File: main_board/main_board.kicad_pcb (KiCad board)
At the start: 2 copper layers, 116.1 x 100.1 mm, 52 parts, among them J1 USB3_A, J11 USB_C_Receptacle_USB2.0, J22 690-019-298-412, J3 Bus_M.2_Socket_M, SW1 Right angle Tact button, U1 AP3441SHE-7B, U12 RT9742SNGV, U2 ASEK-32.768KHZ-L-R-T, U5 74LVC1G07SE-7, U6 AP22653W6

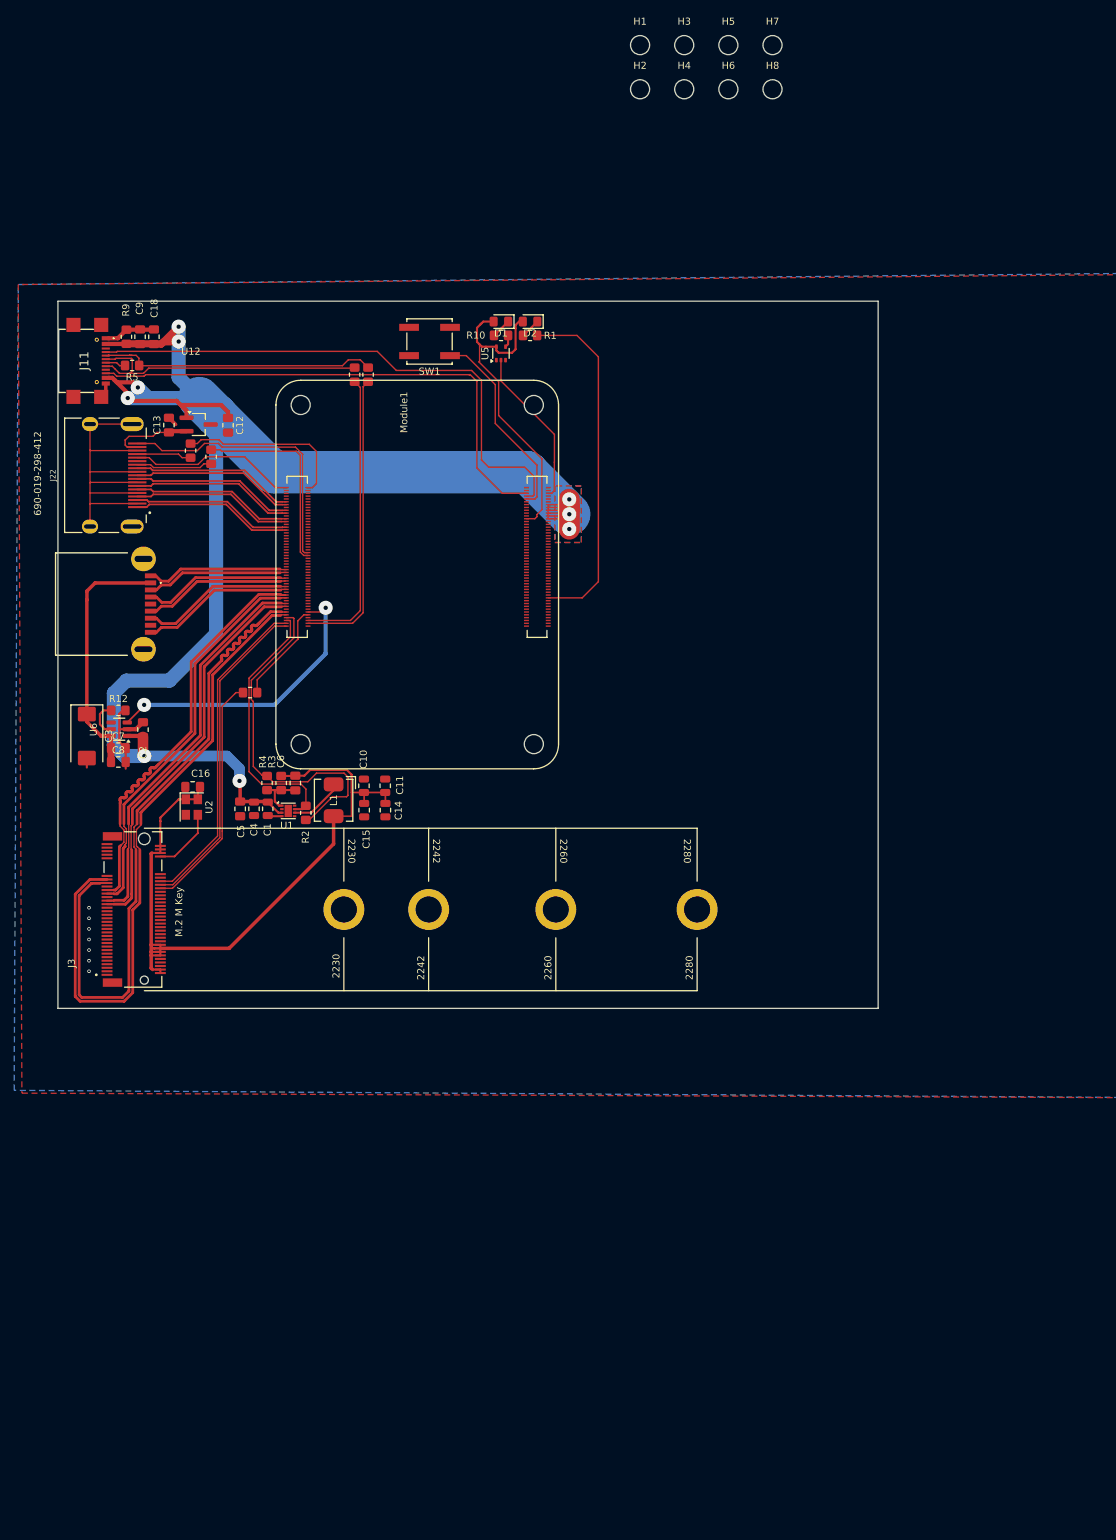
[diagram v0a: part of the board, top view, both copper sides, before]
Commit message: Implement part of power management.
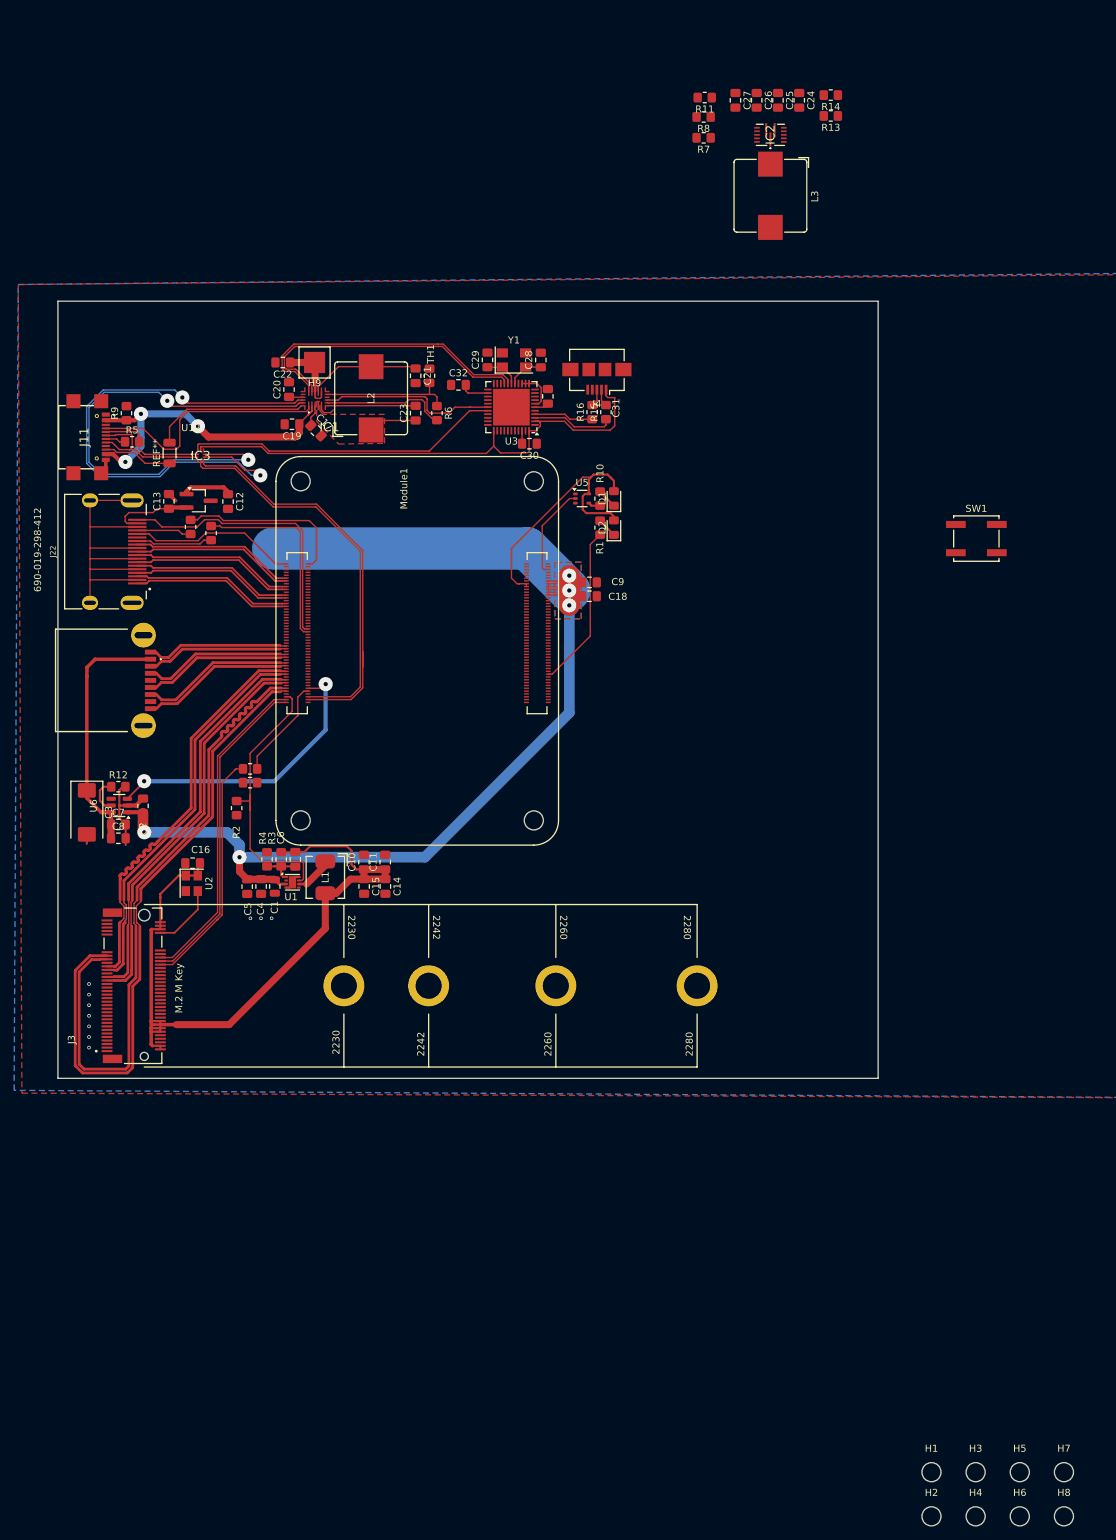
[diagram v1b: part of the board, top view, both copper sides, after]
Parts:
- removed the REF** at (69.9, 30.1)
- removed the REF** at (71.8, 30.1)
- added C17: 10u, Capacitor_SMD:C_0805_2012Metric_Pad1.18x1.45mm_HandSolder, F.Cu at (64.4, 38.0)
- added C19: 1u, Capacitor_SMD:C_0805_2012Metric_Pad1.18x1.45mm_HandSolder, F.Cu at (61.0, 37.1)
- added C20: 4.7u, Capacitor_SMD:C_0805_2012Metric_Pad1.18x1.45mm_HandSolder, F.Cu at (60.6, 32.2)
- added C21: 20u, Capacitor_SMD:C_0805_2012Metric_Pad1.18x1.45mm_HandSolder, F.Cu at (78.5, 30.3)
- added C22: 20u, Capacitor_SMD:C_0805_2012Metric_Pad1.18x1.45mm_HandSolder, F.Cu at (59.7, 28.4)
- added C23: 22n, Capacitor_SMD:C_0805_2012Metric_Pad1.18x1.45mm_HandSolder, F.Cu at (78.5, 35.5)
- added C24: 100n, Capacitor_SMD:C_0805_2012Metric_Pad1.18x1.45mm_HandSolder, F.Cu at (132.8, -8.74)
- added C25: 22n, Capacitor_SMD:C_0805_2012Metric_Pad1.18x1.45mm_HandSolder, F.Cu at (129.8, -8.74)
- added C26: 4.7u, Capacitor_SMD:C_0805_2012Metric_Pad1.18x1.45mm_HandSolder, F.Cu at (126.8, -8.74)
- added C27: 6.8n, Capacitor_SMD:C_0805_2012Metric_Pad1.18x1.45mm_HandSolder, F.Cu at (123.8, -8.74)
- added C28: 22p, Capacitor_SMD:C_0805_2012Metric_Pad1.18x1.45mm_HandSolder, F.Cu at (96.2, 28.0)
- added C29: 22p, Capacitor_SMD:C_0805_2012Metric_Pad1.18x1.45mm_HandSolder, F.Cu at (88.7, 28.0)
- added C30: 100n, Capacitor_SMD:C_0805_2012Metric_Pad1.18x1.45mm_HandSolder, F.Cu at (94.6, 39.9)
- added C31: 1u, Capacitor_SMD:C_0805_2012Metric_Pad1.18x1.45mm_HandSolder, F.Cu at (97.2, 33.2)
- added C32: 1u, Capacitor_SMD:C_0805_2012Metric_Pad1.18x1.45mm_HandSolder, F.Cu at (84.6, 31.6)
- added H9: BAT_PAD, TestPoint:TestPoint_Pad_4.0x4.0mm, F.Cu at (64.2, 28.4)
- added IC1: MP2722GRH-0000-Z, 000_custom:MP2722GRH0000Z, F.Cu at (64.3, 33.5)
- added IC2: MP3429GL-Z, 000_custom:MP3431GLP, F.Cu at (128.8, -3.85)
- added IC3: NX3DV42GU, 000_custom:NX3DV42GU, F.Cu at (48.1, 41.6)
- added J4: USB_B_Micro, Connector_USB:USB_Micro-B_Amphenol_10104110_Horizontal, F.Cu at (104.2, 30.7)
- added L2: L???, Inductor_SMD:L_Bourns_SRP1038C_10.0x10.0mm, F.Cu at (72.2, 33.4)
- added L3: 1.5u, Inductor_SMD:L_Bourns_SRP1038C_10.0x10.0mm, F.Cu at (128.8, 4.78)
- added R11: 6.8K, Resistor_SMD:R_0805_2012Metric_Pad1.20x1.40mm_HandSolder, F.Cu at (119.4, -9.12)
- added R13: rmode, Resistor_SMD:R_0805_2012Metric_Pad1.20x1.40mm_HandSolder, F.Cu at (137.3, -6.52)
- added R14: rmode, Resistor_SMD:R_0805_2012Metric_Pad1.20x1.40mm_HandSolder, F.Cu at (137.3, -9.47)
- added R15: 22R, Resistor_SMD:R_0805_2012Metric_Pad1.20x1.40mm_HandSolder, F.Cu at (105.5, 35.4)
- added R16: 22R, Resistor_SMD:R_0805_2012Metric_Pad1.20x1.40mm_HandSolder, F.Cu at (103.5, 35.4)
- added R6: R=NTC, Resistor_SMD:R_0805_2012Metric_Pad1.20x1.40mm_HandSolder, F.Cu at (81.6, 35.5)
- added R7: Rfb1, Resistor_SMD:R_0805_2012Metric_Pad1.20x1.40mm_HandSolder, F.Cu at (119.3, -3.42)
- added R8: Rfb1, Resistor_SMD:R_0805_2012Metric_Pad1.20x1.40mm_HandSolder, F.Cu at (119.3, -6.37)
- added REF**: R_1206_3216Metric, Resistor_SMD:R_1206_3216Metric, F.Cu at (43.7, 41.2)
- added REF**: R_0805_2012Metric_Pad1.20x1.40mm_HandSolder, Resistor_SMD:R_0805_2012Metric_Pad1.20x1.40mm_HandSolder, F.Cu at (55.1, 87.8)
- added TH1: β = 3435, Resistor_SMD:R_0805_2012Metric_Pad1.20x1.40mm_HandSolder, F.Cu at (80.5, 30.2)
- added U3: ATmega32U4-M, Package_DFN_QFN:QFN-44-1EP_7x7mm_P0.5mm_EP5.2x5.2mm, F.Cu at (92.1, 34.7)
- added Y1: Crystal, Crystal:Crystal_SMD_5032-4Pin_5.0x3.2mm, F.Cu at (92.5, 28.0)
- C10, C11, C14, C15, C4: footprint Capacitor_SMD:C_0805_2012Metric -> Capacitor_SMD:C_0805_2012Metric_Pad1.18x1.45mm_HandSolder
- moved H1 206.2 mm to (151.6, 185.4)
- moved H2 206.2 mm to (151.6, 191.7)
- moved H3 206.2 mm to (157.8, 185.4)
- moved H4 206.2 mm to (157.8, 191.7)
- moved H5 206.2 mm to (164.1, 185.4)
- moved H6 206.2 mm to (164.1, 191.7)
- moved H7 206.2 mm to (170.3, 185.4)
- moved H8 206.2 mm to (170.3, 191.7)
- moved SW1 82.3 mm to (157.9, 53.3), turned to 180 degrees
- moved C9 72.5 mm to (103.1, 59.5), turned to 0 degrees
- moved C18 71.8 mm to (103.1, 61.5), turned to 0 degrees
- moved D2 31.5 mm to (106.6, 51.8), turned to 90 degrees
- moved D1 29.7 mm to (106.6, 47.6), turned to 90 degrees
- moved R1 29.0 mm to (104.6, 51.8), turned to -90 degrees
- moved R10 27.0 mm to (104.6, 47.6), turned to -90 degrees
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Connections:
- net /+3.3v renamed /CM5_GPIO/+3.3v
- net /CM5_GPIO ( Ethernet, GPIO, SDCARD)/+1.8v renamed /CM5_GPIO/+1.8v
- net /CM5_GPIO ( Ethernet, GPIO, SDCARD)/EEPROM_nWP renamed /CM5_GPIO/EEPROM_nWP
- net /CM5_GPIO ( Ethernet, GPIO, SDCARD)/GPIO10 renamed /CM5_GPIO/GPIO10
- net /CM5_GPIO ( Ethernet, GPIO, SDCARD)/GPIO11 renamed /CM5_GPIO/GPIO11
- net /CM5_GPIO ( Ethernet, GPIO, SDCARD)/GPIO12 renamed /CM5_GPIO/GPIO12
- net /CM5_GPIO ( Ethernet, GPIO, SDCARD)/GPIO13 renamed /CM5_GPIO/GPIO13
- net /CM5_GPIO ( Ethernet, GPIO, SDCARD)/GPIO14 renamed /CM5_GPIO/GPIO14
- net /CM5_GPIO ( Ethernet, GPIO, SDCARD)/GPIO15 renamed /CM5_GPIO/GPIO15
- net /CM5_GPIO ( Ethernet, GPIO, SDCARD)/GPIO16 renamed /CM5_GPIO/GPIO16
- net /CM5_GPIO ( Ethernet, GPIO, SDCARD)/GPIO17 renamed /CM5_GPIO/GPIO17
- net /CM5_GPIO ( Ethernet, GPIO, SDCARD)/GPIO18 renamed /CM5_GPIO/GPIO18
- net /CM5_GPIO ( Ethernet, GPIO, SDCARD)/GPIO19 renamed /CM5_GPIO/GPIO19
- net /CM5_GPIO ( Ethernet, GPIO, SDCARD)/GPIO2 renamed /CM5_GPIO/GPIO2
- net /CM5_GPIO ( Ethernet, GPIO, SDCARD)/GPIO20 renamed /CM5_GPIO/GPIO20
- net /CM5_GPIO ( Ethernet, GPIO, SDCARD)/GPIO21 renamed /CM5_GPIO/GPIO21
- net /CM5_GPIO ( Ethernet, GPIO, SDCARD)/GPIO22 renamed /CM5_GPIO/GPIO22
- net /CM5_GPIO ( Ethernet, GPIO, SDCARD)/GPIO23 renamed /CM5_GPIO/GPIO23
- net /CM5_GPIO ( Ethernet, GPIO, SDCARD)/GPIO24 renamed /CM5_GPIO/GPIO24
- net /CM5_GPIO ( Ethernet, GPIO, SDCARD)/GPIO25 renamed /CM5_GPIO/GPIO25
- net /CM5_GPIO ( Ethernet, GPIO, SDCARD)/GPIO26 renamed /CM5_GPIO/GPIO26
- net /CM5_GPIO ( Ethernet, GPIO, SDCARD)/GPIO27 renamed /CM5_GPIO/GPIO27
- net /CM5_GPIO ( Ethernet, GPIO, SDCARD)/GPIO3 renamed /CM5_GPIO/GPIO3
- net /CM5_GPIO ( Ethernet, GPIO, SDCARD)/GPIO4 renamed /CM5_GPIO/GPIO4
- net /CM5_GPIO ( Ethernet, GPIO, SDCARD)/GPIO5 renamed /CM5_GPIO/GPIO5
- net /CM5_GPIO ( Ethernet, GPIO, SDCARD)/GPIO6 renamed /CM5_GPIO/GPIO6
- net /CM5_GPIO ( Ethernet, GPIO, SDCARD)/GPIO7 renamed /CM5_GPIO/GPIO7
- net /CM5_GPIO ( Ethernet, GPIO, SDCARD)/GPIO8 renamed /CM5_GPIO/GPIO8
- net /CM5_GPIO ( Ethernet, GPIO, SDCARD)/GPIO9 renamed /CM5_GPIO/GPIO9
- net /CM5_GPIO ( Ethernet, GPIO, SDCARD)/LED_nACT renamed /CM5_GPIO/LED_nACT
- net /CM5_GPIO ( Ethernet, GPIO, SDCARD)/PMIC_ENABLE renamed /CM5_GPIO/PMIC_ENABLE
- net /CM5_GPIO ( Ethernet, GPIO, SDCARD)/PWR_BUT renamed /CM5_GPIO/PWR_BUT
- net /CM5_GPIO ( Ethernet, GPIO, SDCARD)/nPWR_LED renamed /CM5_GPIO/nPWR_LED
- J11 pad A4: /+5v -> /Battery management/VIN
- J11 pad A5: /CC1 -> /Battery management/CC1
- J11 pad A6: /USB2_P -> /Battery management/USB2_P
- J11 pad A7: /USB2_N -> /Battery management/USB2_N
- J11 pad B4: /+5v -> /Battery management/VIN
- J11 pad B5: /CC2 -> /Battery management/CC2
- J11 pad B6: /USB2_P -> /Battery management/USB2_P
- J11 pad B7: /USB2_N -> /Battery management/USB2_N
- Module1 pad 100: unconnected-(Module1A-CAM_GPIO1-Pad100) -> /CM5_GPIO/GPIO1
- Module1 pad 103: /USB2_N -> /Battery management/USBC_MX1_USB2_N
- Module1 pad 105: /USB2_P -> /Battery management/USBC_MX1_USB2_P
- Module1 pad 94: /CC1 -> unconnected-(Module1A-CC1-Pad94)
- Module1 pad 96: /CC2 -> unconnected-(Module1A-CC2-Pad96)
- Module1 pad 97: unconnected-(Module1A-CAM_GPIO0-Pad97) -> /CM5_GPIO/GPIO0
- R5 pad 1: /USB2_N -> /Battery management/USB2_N
- R5 pad 2: /USB2_N -> /Battery management/USB2_N
- R9 pad 1: /+5v -> /Battery management/VIN
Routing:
- net /USB2_N: track 83.9 -> 0.00 mm
- net /USB2_P: track 82.1 -> 0.00 mm
- net /CC1: track 78.3 -> 0.00 mm
- net /Battery management/USBC_MX2_USB2_P: track 0.00 -> 76.5 mm, vias 0 -> 2
- net /CC2: track 73.7 -> 0.00 mm
- net /Battery management/USBC_MX2_USB2_N: track 0.00 -> 70.6 mm, vias 0 -> 2
- net /Battery management/USBC_MX1_USB2_N: track 0.00 -> 58.0 mm
- net /Battery management/USBC_MX1_USB2_P: track 0.00 -> 55.5 mm
- net GND: track 133.2 -> 80.0 mm, vias 7 -> 10
- net /Battery management/VIN: track 0.00 -> 45.8 mm, vias 0 -> 3
- net /Battery management/OTG_SW: track 0.00 -> 44.7 mm
- net /Battery management/SCL: track 0.00 -> 42.7 mm
- net /Battery management/SDA: track 0.00 -> 41.6 mm
- net /Battery management/CC1: track 0.00 -> 35.0 mm
- net /Battery management/CC2: track 0.00 -> 31.8 mm
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- added copper zone on F.Cu, net Net-(IC1-SW)
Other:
- board size 116.1 x 100.1 mm -> 116.1 x 110 mm

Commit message: More power management goodness
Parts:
- removed J11: USB_C_Receptacle_USB2.0, Library:USB421603A
- removed R13, R14: rmode, Resistor_SMD:R_0805_2012Metric_Pad1.20x1.40mm_HandSolder
- removed REF**: R_1206_3216Metric, Resistor_SMD:R_1206_3216Metric
- removed REF** (x4): R_0805_2012Metric_Pad1.20x1.40mm_HandSolder, Resistor_SMD:R_0805_2012Metric_Pad1.20x1.40mm_HandSolder
- added C33: 22u, Capacitor_SMD:C_0805_2012Metric_Pad1.18x1.45mm_HandSolder, F.Cu at (112.3, 38.9)
- added C34: 22u, Capacitor_SMD:C_0805_2012Metric_Pad1.18x1.45mm_HandSolder, F.Cu at (112.3, 40.9)
- added C35: 22u, Capacitor_SMD:C_0805_2012Metric_Pad1.18x1.45mm_HandSolder, F.Cu at (112.3, 42.8)
- added C36: 22u, Capacitor_SMD:C_0805_2012Metric_Pad1.18x1.45mm_HandSolder, F.Cu at (128.5, 35.1)
- added C37: 22u, Capacitor_SMD:C_0805_2012Metric_Pad1.18x1.45mm_HandSolder, F.Cu at (128.6, 37.1)
- added C38: 22u, Capacitor_SMD:C_0805_2012Metric_Pad1.18x1.45mm_HandSolder, F.Cu at (128.6, 39.0)
- added C39: 100n, Capacitor_SMD:C_0805_2012Metric_Pad1.18x1.45mm_HandSolder, F.Cu at (124.2, 34.1)
- added J5: USB_C_Receptacle_USB2.0, 000_custom:USB421603A, F.Cu at (31.3, 39.0)
- added JMP: R_0805_2012Metric_Pad1.20x1.40mm_HandSolder, Resistor_SMD:R_0805_2012Metric_Pad1.20x1.40mm_HandSolder, F.Cu at (55.1, 85.9)
- added JMP: R_0805_2012Metric_Pad1.20x1.40mm_HandSolder, Resistor_SMD:R_0805_2012Metric_Pad1.20x1.40mm_HandSolder, F.Cu at (49.6, 52.5)
- added JMP: R_1206_3216Metric, Resistor_SMD:R_1206_3216Metric, F.Cu at (43.7, 41.2)
- added JMP: R_0805_2012Metric_Pad1.20x1.40mm_HandSolder, Resistor_SMD:R_0805_2012Metric_Pad1.20x1.40mm_HandSolder, F.Cu at (46.7, 51.6)
- added R17: 15K, Resistor_SMD:R_0805_2012Metric_Pad1.20x1.40mm_HandSolder, F.Cu at (121.3, 28.3)
- moved R4 76.6 mm to (134.0, 102.3), turned to 0 degrees
- moved C5 75.6 mm to (130.2, 99.5), turned to 180 degrees
- moved R3 74.8 mm to (134.0, 104.3), turned to 180 degrees
- moved C4 73.6 mm to (130.2, 101.5), turned to 180 degrees
- moved R2 73.5 mm to (125.7, 103.7), turned to 90 degrees
- moved C6 72.9 mm to (134.0, 106.3), turned to 180 degrees
- moved C1 71.6 mm to (130.2, 103.4), turned to 180 degrees
- moved U1 69.8 mm to (130.8, 105.9), turned to -90 degrees
- moved H9 66.9 mm to (2.52, 2.52), turned to 0 degrees
- moved L1 66.4 mm to (131.5, 110.6), turned to 180 degrees
- moved C10 64.7 mm to (133.7, 116.0), turned to 0 degrees
- moved C11 62.7 mm to (133.7, 119.0), turned to 0 degrees
- moved C15 60.5 mm to (130.2, 116.1), turned to 180 degrees
- moved C14 58.3 mm to (130.2, 119.1), turned to 180 degrees
- moved R11 52.2 mm to (125.5, 42.8)
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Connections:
- net /CM5_GPIO/PMIC_ENABLE renamed /CM5_GPIO/CM5_PMIC_EN
- C1 pad 1: /+5v -> /Battery management/+5V
- C12 pad 1: /+5v -> /Battery management/+5V
- C18 pad 1: /+5v -> /Battery management/+5V
- C2 pad 1: /+5v -> /Battery management/+5V
- C21 pad 1: Net-(IC1-SYS) -> /Battery management/V_SYS
- C32 pad 2: /+5v -> /Battery management/V_SYS
- C4 pad 1: /+5v -> /Battery management/+5V
- C5 pad 1: /+5v -> /Battery management/+5V
- C9 pad 1: /+5v -> /Battery management/+5V
- H9 pad 1: /Battery management/VBAT -> (no net)
- IC1 pad 13: Net-(IC1-SYS) -> /Battery management/V_SYS
- IC1 pad 15: /Battery management/SDA -> /Battery management/IIC_SCL
- IC1 pad 16: /Battery management/SCL -> /Battery management/IIC_SDA
- IC2 pad 10: Net-(IC2-MODE) -> unconnected-(IC2-MODE-Pad10)
- IC2 pad 11: /Battery management/VBAT -> Net-(IC2-EN)
- IC2 pad 8: /+5v -> /Battery management/+5V
- IC3 pad 9: /+5v -> /Battery management/V_SYS
- J4 pad 1: /+5v -> /Battery management/V_SYS
- L2 pad 2: Net-(IC1-SYS) -> /Battery management/V_SYS
- Module1 pad 100: /CM5_GPIO/GPIO1 -> /Battery management/IIC_SDA
- Module1 pad 101: /CM5_HighSpeed/USBOTG_ID -> unconnected-(Module1B-USB_OTG_ID-Pad101)
- Module1 pad 77: /+5v -> /Battery management/+5V
- Module1 pad 79: /+5v -> /Battery management/+5V
- Module1 pad 81: /+5v -> /Battery management/+5V
- Module1 pad 83: /+5v -> /Battery management/+5V
- Module1 pad 85: /+5v -> /Battery management/+5V
- Module1 pad 87: /+5v -> /Battery management/+5V
- Module1 pad 97: /CM5_GPIO/GPIO0 -> /Battery management/IIC_SCL
- R8 pad 2: /+5v -> /Battery management/+5V
- SW1 pad 2: /CM5_GPIO/PWR_BUT -> unconnected-(SW1-Pad2)
- U1 pad 3: /+5v -> /Battery management/+5V
- U12 pad 1: /+5v -> /Battery management/+5V
- U3 pad 11: unconnected-(U3-PB3-Pad11) -> Net-(IC2-EN)
- U3 pad 12: /+5v -> /Battery management/V_SYS
- U3 pad 13: /+5v -> /Battery management/V_SYS
- U3 pad 14: /+5v -> /Battery management/V_SYS
- U3 pad 18: /Battery management/SCL -> /Battery management/IIC_SDA
- U3 pad 19: /Battery management/SDA -> /Battery management/IIC_SCL
- U3 pad 2: /+5v -> /Battery management/V_SYS
- U3 pad 24: /+5v -> /Battery management/V_SYS
- U3 pad 34: /+5v -> /Battery management/V_SYS
- U3 pad 44: /+5v -> /Battery management/V_SYS
- U3 pad 7: /+5v -> /Battery management/V_SYS
- U6 pad 1: /+5v -> /Battery management/+5V
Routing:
- net /Battery management/+5V: track 0.00 -> 527.4 mm
- net /+5v: track 262.1 -> 0.00 mm, vias 5 -> 0
- net /Battery management/VBAT: track 10.2 -> 142.8 mm, vias 0 -> 4
- net /Battery management/V_SYS: track 0.00 -> 87.6 mm, vias 0 -> 3
- net /CM5_HighSpeed/PCIE_PWR_EN: track 40.1 -> 118.1 mm
- net /PCIe-M2/M2_3v3: track 109.5 -> 162.4 mm
- net GND: track 80.0 -> 32.2 mm, vias 10 -> 15
- net Net-(IC2-EN): track 0.00 -> 47.0 mm
- net /Battery management/USBC_MX2_USB2_P: track 76.5 -> 30.8 mm
- net /Battery management/SCL: track 42.7 -> 0.00 mm
- net /Battery management/SDA: track 41.6 -> 0.00 mm
- net /Battery management/USBC_MX2_USB2_N: track 70.6 -> 30.5 mm
- net /Battery management/IIC_SDA: track 0.00 -> 38.4 mm
- net /Battery management/IIC_SCL: track 0.00 -> 37.0 mm
- net /CM5_GPIO/+3.3v: track 38.7 -> 20.4 mm
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- added copper zone on F.Cu, net /Battery management/+5V
- added copper zone on F.Cu, net /Battery management/VBAT
- added copper zone on B.Cu, net /Battery management/V_SYS
- added copper zone on F.Cu, net /Battery management/V_SYS
- added copper zone on F.Cu, net Net-(IC2-SW)
- removed copper zone on B.Cu, net /+5v
- removed copper zone on F.Cu, net /+5v
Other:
- board size 116.1 x 110 mm -> 160 x 110 mm
